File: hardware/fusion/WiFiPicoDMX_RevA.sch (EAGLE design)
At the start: 36 parts, among them J1 PANEL XLR-5: COM,-,+,SHELL, J2 PANEL DIN-5 MIDI IN, J3 FREE GPIO PADS, J4 ANALOG PADS, J5 RESERVED SIGNAL TEST PADS, J6 POWER/DMX TEST PADS, SW1 RESET (NO), U1 Raspberry Pi Pico 2 W, U2 ISOW1412DFMR, U3 6N138-500E

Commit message: Add validated hardware net lists
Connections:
- net 3V3_LOGIC renamed VCC_3V3_LOGIC
- net 5V_DMX_FUSED renamed VDD_5V_ISOW_FUSED
- net 5V_DMX_ISO renamed VCC_5V_DMX_ISO
- net 5V_DMX_ISO_RAW renamed VISO_5V_CONVERTER
- net 5V_VBUS_RAW renamed VBUS_5V_USB
- net DMX_LED_DRIVE renamed DMX_LED_ANODE
- net DMX_TRANSCEIVER_MINUS renamed DMX_TRX_MINUS
- net DMX_TRANSCEIVER_PLUS renamed DMX_TRX_PLUS
- net GND_DMX_ISO_RAW renamed GND_DMX_CONVERTER
- net GPIO0_FREE renamed GPIO0_EXP
- net GPIO10_FREE renamed GPIO10_EXP
- net GPIO11_FREE renamed GPIO11_EXP
- net GPIO12_FREE renamed GPIO12_EXP
- net GPIO13_FREE renamed GPIO13_EXP
- net GPIO14_FREE renamed GPIO14_EXP
- net GPIO15_FREE renamed GPIO15_EXP
- net GPIO16_FREE renamed GPIO16_EXP
- net GPIO17_FREE renamed GPIO17_EXP
- net GPIO18_FREE renamed GPIO18_EXP
- net GPIO19_FREE renamed GPIO19_EXP
- net GPIO1_FREE renamed GPIO1_EXP
- net GPIO20_FREE renamed GPIO20_EXP
- net GPIO21_FREE renamed GPIO21_EXP
- net GPIO22_FREE renamed GPIO22_EXP
- net GPIO8_FREE renamed GPIO8_EXP
- net GPIO9_FREE renamed GPIO9_EXP
- net ISOW_IN_NC renamed NC_U2_PIN14_IN
- net ISOW_OUT_NC renamed NC_U2_PIN7_OUT
- net MIDI_DIN_PIN1_NC renamed MIDI_DIN_PIN1_SPARE
- net MIDI_DIN_PIN3_NC renamed MIDI_DIN_PIN3_SPARE
- net MIDI_LED_ANODE renamed MIDI_OPTO_LED_ANODE
- net MIDI_LED_CATHODE renamed MIDI_OPTO_LED_CATHODE
- net PICO_3V3_EN renamed PICO_SMPS_EN
- net PICO_RUN renamed PICO_RUN_N
- net PWR_LED_DRIVE renamed PWR_LED_ANODE
- net U3_NC1 renamed NC_U3_PIN1
- net U3_NC4 renamed NC_U3_PIN4

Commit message: docs(hardware): select HCPL-0700 MIDI optocoupler
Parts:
- L1: value OPTIONAL CMC - DNP -> ACT45B-510-2P-TL003 - DNP
- SW1: value RESET (NO) -> PTS810SJM250SMTR LFS RESET (NO)
- U3: value 6N138-500E -> HCPL-0700-500E; device WiFiPicoDMX_RevA_embedded:6N138_500E -> WiFiPicoDMX_RevA_embedded:HCPL_0700_500E
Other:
- note added: "Default: FIT R10/R11 (0R), DNP L1. L1 option is TDK ACT45B-510-2P-TL003; fit it only after EMC/signal-integrity testing."
- note added: "HCPL-0700 output side uses 5V VCC with a 3.3V output pull-up. Verify timing/CTR on the assembled prototype."
- note removed: "6N138 output side uses 5V VCC with a 3.3V output pull-up. Verify timing/CTR on the assembled prototype."
- note removed: "FIT R10/R11 (0R) and DNP L1 until a common-mode choke is selected by EMC/signal-integrity testing."
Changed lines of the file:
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@@
         <part name="U1" library="WiFiPicoDMX_RevA_embedded" deviceset="PICO2W" device="" value="Raspberry Pi Pico 2 W"/>
         <part name="F1" library="WiFiPicoDMX_RevA_embedded" deviceset="PPTC1206" device="" value="1206L050YR 0.5A HOLD"/>
-        <part name="SW1" library="WiFiPicoDMX_RevA_embedded" deviceset="SWITCH_SMD" device="" value="RESET (NO)"/>
+        <part name="SW1" library="WiFiPicoDMX_RevA_embedded" deviceset="SWITCH_SMD" device="" value="PTS810SJM250SMTR LFS RESET (NO)"/>
         <part name="R8" library="WiFiPicoDMX_RevA_embedded" deviceset="RES0603" device="" value="1k"/>
         <part name="D3" library="WiFiPicoDMX_RevA_embedded" deviceset="LED0603" device="" value="PWR GREEN"/>
@@
         <part name="C5" library="WiFiPicoDMX_RevA_embedded" deviceset="CAP0805" device="" value="10u X7R VISOOUT"/>
         <part name="C6" library="WiFiPicoDMX_RevA_embedded" deviceset="CAP0402" device="" value="100n VISOIN"/>
-        <part name="L1" library="WiFiPicoDMX_RevA_embedded" deviceset="CMC_OPTION" device="" value="OPTIONAL CMC - DNP"/>
+        <part name="L1" library="WiFiPicoDMX_RevA_embedded" deviceset="CMC_OPTION" device="" value="ACT45B-510-2P-TL003 - DNP"/>
         <part name="R10" library="WiFiPicoDMX_RevA_embedded" deviceset="RES0603" device="" value="0R CMC BYPASS FIT"/>
         <part name="R11" library="WiFiPicoDMX_RevA_embedded" deviceset="RES0603" device="" value="0R CMC BYPASS FIT"/>
@@
         <part name="R5" library="WiFiPicoDMX_RevA_embedded" deviceset="RES0603" device="" value="220R"/>
         <part name="D2" library="WiFiPicoDMX_RevA_embedded" deviceset="DIODE_SOD323" device="" value="1N4148WS-E3-08"/>
-        <part name="U3" library="WiFiPicoDMX_RevA_embedded" deviceset="6N138_500E" device="" value="6N138-500E"/>
+        <part name="U3" library="WiFiPicoDMX_RevA_embedded" deviceset="HCPL_0700_500E" device="" value="HCPL-0700-500E"/>
         <part name="R6" library="WiFiPicoDMX_RevA_embedded" deviceset="RES0603" device="" value="4.7k OUTPUT PULLUP"/>
         <part name="R7" library="WiFiPicoDMX_RevA_embedded" deviceset="RES0603" device="" value="47k BASE SPEEDUP"/>
@@
                   <plain>
                     <text x="20.32" y="187.96" size="2.54" layer="91" ratio="15">WiFiPicoDMX Rev. A — Reinforced-isolated DMX/RDM output</text>
-                    <text x="20.32" y="20.32" size="1.778" layer="91" ratio="12">FIT R10/R11 (0R) and DNP L1 until a common-mode choke is selected by EMC/signal-integrity testing.</text>
+                    <text x="20.32" y="20.32" size="1.778" layer="91" ratio="12">Default: FIT R10/R11 (0R), DNP L1. L1 option is TDK ACT45B-510-2P-TL003; fit it only after EMC/signal-integrity testing.</text>
                     <text x="20.32" y="15.24" size="1.778" layer="91" ratio="12">No permanent 120R termination: terminate only at the far end of the DMX cable.</text>
                     <text x="20.32" y="10.16" size="1.778" layer="91" ratio="12">Keep GND_LOGIC and GND_DMX_ISO separate. Preserve TI isolation keep-outs and place bypass parts per TI layout.</text>
@@
                     <text x="20.32" y="187.96" size="2.54" layer="91" ratio="15">WiFiPicoDMX Rev. A — Isolated MIDI IN</text>
                     <text x="20.32" y="20.32" size="1.778" layer="91" ratio="12">J2 exposes all five panel DIN pins. Pins 1/3 are NC; pin 2 shield treatment remains configurable.</text>
-                    <text x="20.32" y="15.24" size="1.778" layer="91" ratio="12">6N138 output side uses 5V VCC with a 3.3V output pull-up. Verify timing/CTR on the assembled prototype.</text>
+                    <text x="20.32" y="15.24" size="1.778" layer="91" ratio="12">HCPL-0700 output side uses 5V VCC with a 3.3V output pull-up. Verify timing/CTR on the assembled prototype.</text>
                     <text x="20.32" y="10.16" size="1.778" layer="91" ratio="12">The DIN input current loop remains galvanically isolated from GND_LOGIC.</text>
                   </plain>

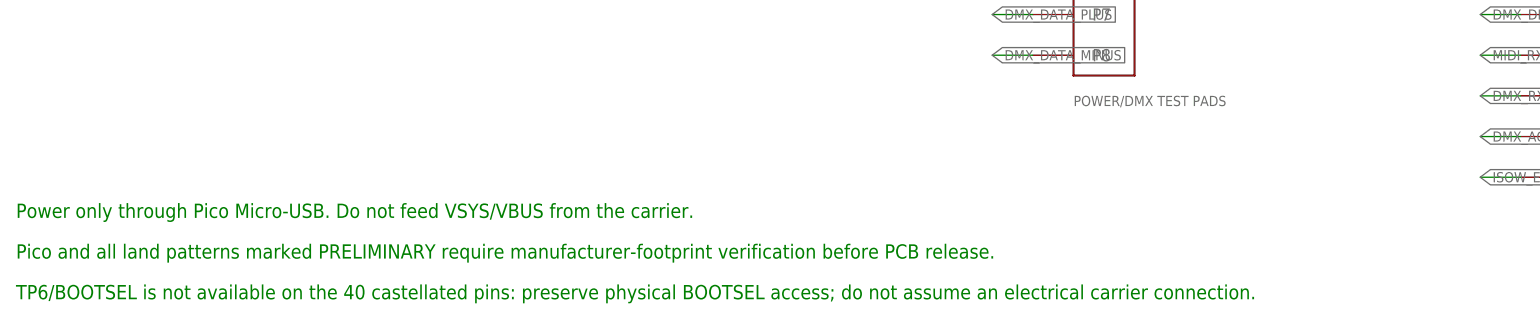
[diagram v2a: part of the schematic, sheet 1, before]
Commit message: feat(hardware): generate schematic from Fusion library
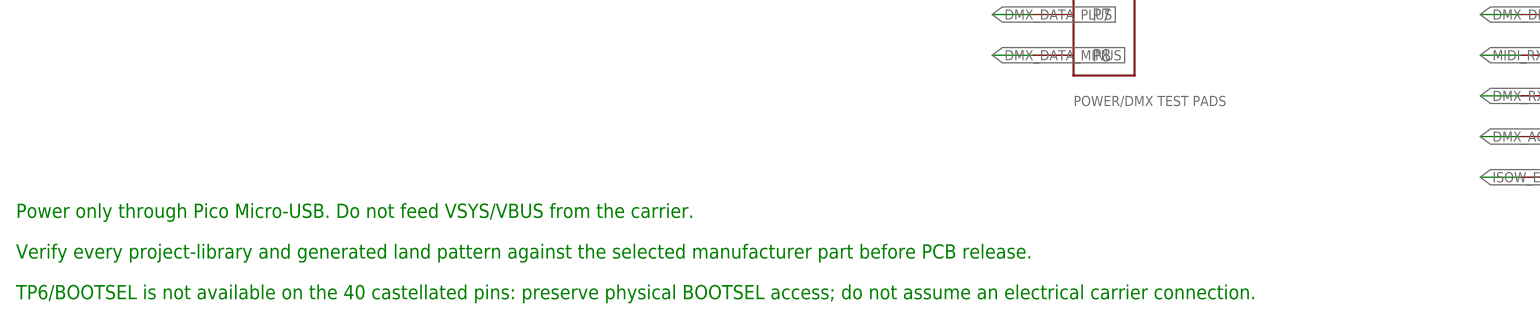
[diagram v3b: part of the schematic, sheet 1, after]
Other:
- note added: "Verify every project-library and generated land pattern against the selected manufacturer part before PCB release."
- note removed: "Pico and all land patterns marked PRELIMINARY require manufacturer-footprint verification before PCB release."
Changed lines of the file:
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@@
                     <text x="20.32" y="187.96" size="2.54" layer="91" ratio="15">WiFiPicoDMX Rev. A — Controller, power, controls and expansion</text>
                     <text x="20.32" y="15.24" size="1.778" layer="91" ratio="12">Power only through Pico Micro-USB. Do not feed VSYS/VBUS from the carrier.</text>
-                    <text x="20.32" y="10.16" size="1.778" layer="91" ratio="12">Pico and all land patterns marked PRELIMINARY require manufacturer-footprint verification before PCB release.</text>
+                    <text x="20.32" y="10.16" size="1.778" layer="91" ratio="12">Verify every project-library and generated land pattern against the selected manufacturer part before PCB release.</text>
                     <text x="20.32" y="5.08" size="1.778" layer="91" ratio="12">TP6/BOOTSEL is not available on the 40 castellated pins: preserve physical BOOTSEL access; do not assume an electrical carrier connection.</text>
                   </plain>

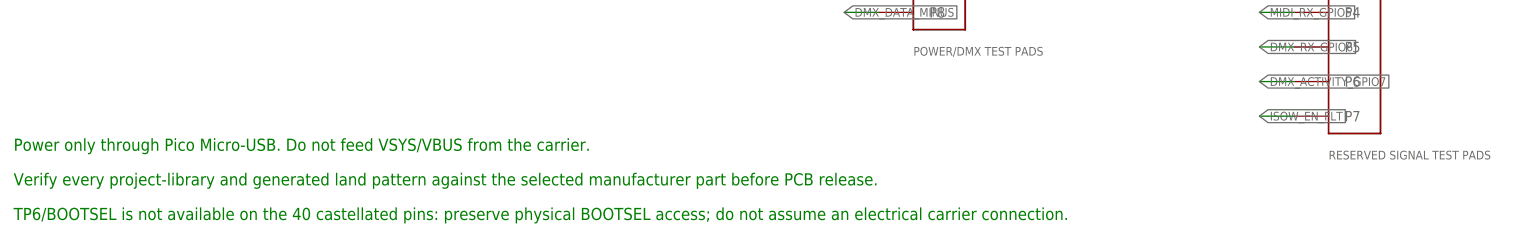
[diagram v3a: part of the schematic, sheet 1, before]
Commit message: fix(hardware): restore Fusion library models and Pico footprint
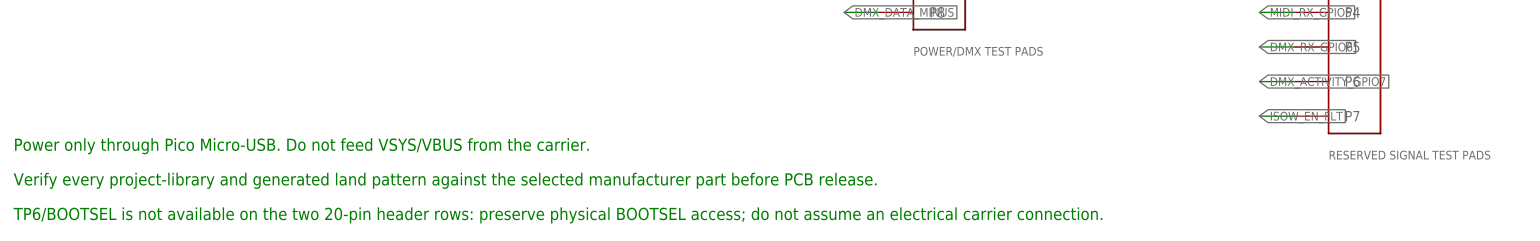
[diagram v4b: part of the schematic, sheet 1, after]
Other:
- note added: "TP6/BOOTSEL is not available on the two 20-pin header rows: preserve physical BOOTSEL access; do not assume an electrical carrier connection."
- note removed: "TP6/BOOTSEL is not available on the 40 castellated pins: preserve physical BOOTSEL access; do not assume an electrical carrier connection."
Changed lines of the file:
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@@
                     <text x="20.32" y="15.24" size="1.778" layer="91" ratio="12">Power only through Pico Micro-USB. Do not feed VSYS/VBUS from the carrier.</text>
                     <text x="20.32" y="10.16" size="1.778" layer="91" ratio="12">Verify every project-library and generated land pattern against the selected manufacturer part before PCB release.</text>
-                    <text x="20.32" y="5.08" size="1.778" layer="91" ratio="12">TP6/BOOTSEL is not available on the 40 castellated pins: preserve physical BOOTSEL access; do not assume an electrical carrier connection.</text>
+                    <text x="20.32" y="5.08" size="1.778" layer="91" ratio="12">TP6/BOOTSEL is not available on the two 20-pin header rows: preserve physical BOOTSEL access; do not assume an electrical carrier connection.</text>
                   </plain>
                   <instances>

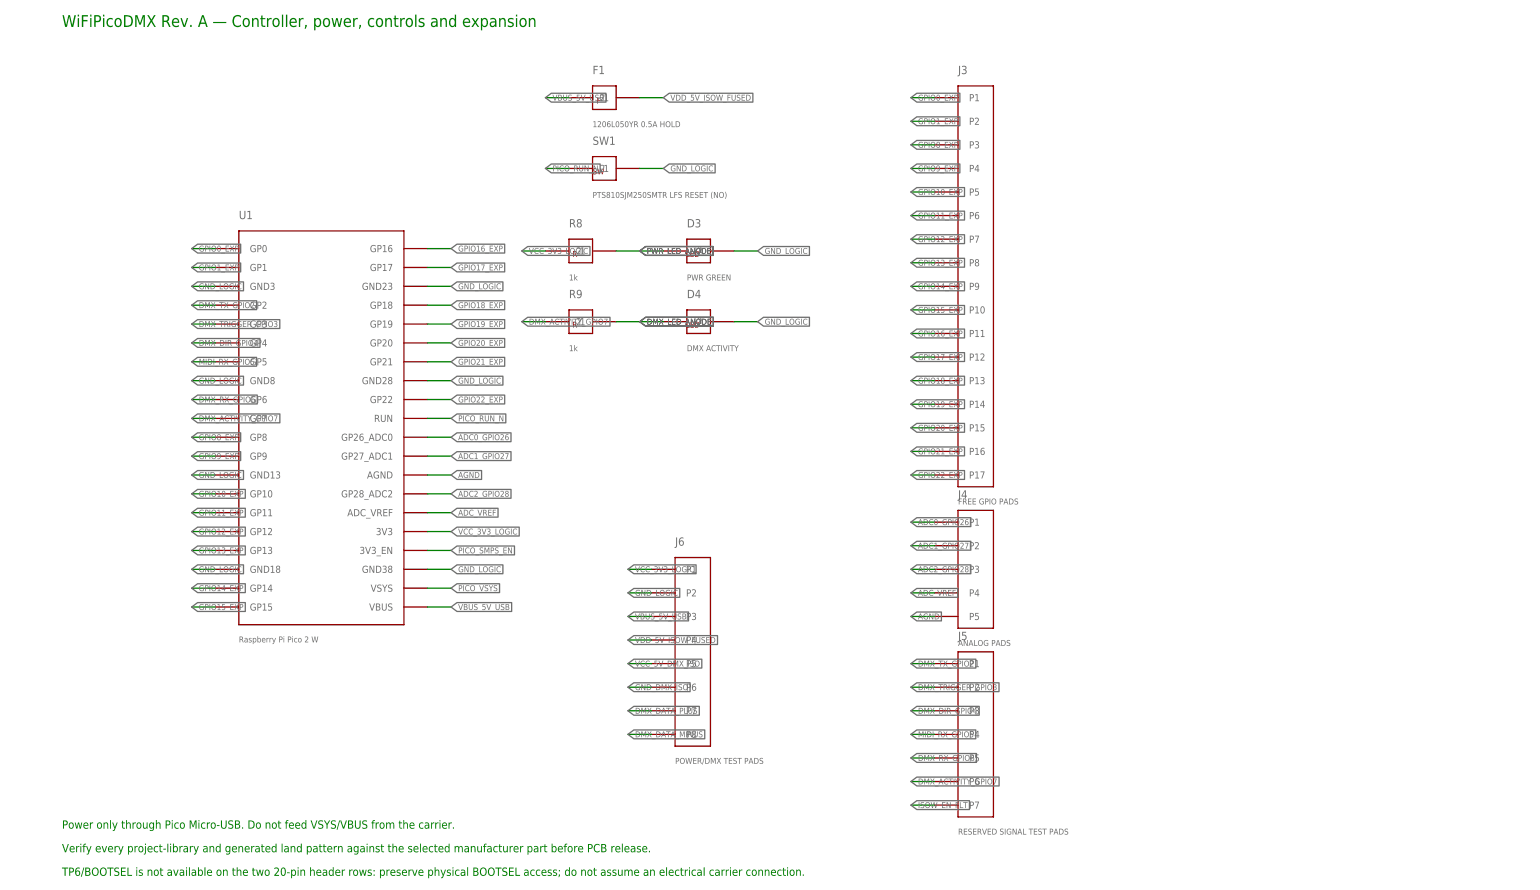
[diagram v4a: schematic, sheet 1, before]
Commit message: fix(hardware): improve generated Fusion schematic layout
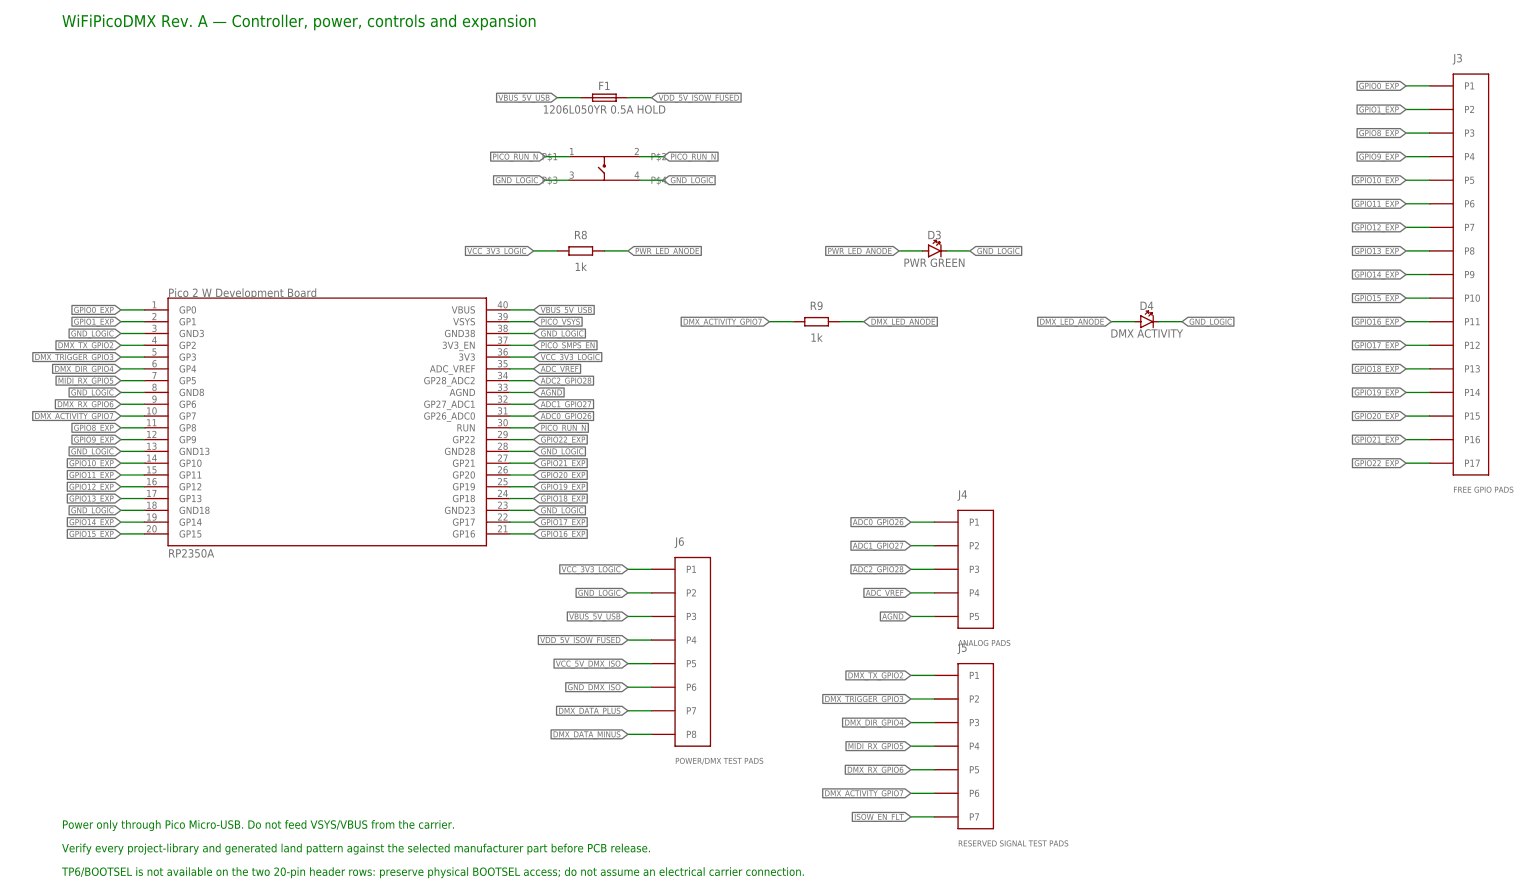
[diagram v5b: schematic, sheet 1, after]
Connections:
- net GND_LOGIC: now also SW1.P$3, SW1.P$4; no longer SW1.2
- net PICO_RUN_N: now also SW1.P$1, SW1.P$2; no longer SW1.1
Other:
- moved on the sheet: D1, J1, J3, J5, L1

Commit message: hardware: freeze Rev A passive BOM
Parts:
- added C8: 1uF 50V 10% X5R 0603 CL10A105KB8NNNC VDD 2-4mm, WiFiPicoDMX_RevA_embedded:CAP0603
- added C9: 1uF 50V 10% X5R 0603 CL10A105KB8NNNC VISOOUT 2-4mm, WiFiPicoDMX_RevA_embedded:CAP0603
- C1: value 100n VIO -> 100nF 16V 10% X7R 0402 CL05B104KO5NNNC VIO
- C2: value 10n VDD <=1mm -> 10nF 50V 10% X7R 0402 0402B103K500CT VDD <1mm
- C3: value 10u X7R VDD -> 10uF 35V 10% X5R 0805 GRM21BR6YA106KE43L VDD
- C4: value 10n VISOOUT <=1mm -> 10nF 50V 10% X7R 0402 0402B103K500CT VISOOUT <1mm
- C5: value 10u X7R VISOOUT -> 10uF 35V 10% X5R 0805 GRM21BR6YA106KE43L VISOOUT
- C6: value 100n VISOIN -> 100nF 16V 10% X7R 0402 CL05B104KO5NNNC VISOIN
- C7: value 100n VCC -> 100nF 16V 10% X7R 0402 CL05B104KO5NNNC MIDI VCC
- D3: value PWR GREEN -> PWR GREEN Lite-On LTST-C190KGKT
- D4: value DMX ACTIVITY -> DMX YELLOW Lite-On LTST-C190KSKT
- R1: value 100k D PULLUP -> 100k 1% 0.063W 0402 Yageo RC0402FR-07100KL
- R10, R11: value 0R CMC BYPASS FIT -> 0R 5% 0.1W 0603 Yageo RC0603JR-070RL CMC BYPASS FIT
- R2: value 10k DIR PULLDOWN -> 10k 1% 0.063W 0402 Yageo RC0402FR-0710KL
- R3: value 10k EN/FLT PULLUP -> 10k 1% 0.063W 0402 Yageo RC0402FR-0710KL
- R4, R5: value 220R -> 220R 1% 0.1W 0603 Yageo RC0603FR-07220RL
- R6: value 4.7k OUTPUT PULLUP -> 4.7k 1% 0.1W 0603 Yageo RC0603FR-074K7L
- R7: value 47k BASE SPEEDUP -> 47k 1% 0.1W 0603 Yageo RC0603FR-0747KL
- R8, R9: value 1k -> 1k 1% 0.1W 0603 Yageo RC0603FR-071KL
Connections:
- net GND_DMX_CONVERTER: now also C9.2
- net GND_LOGIC: now also C8.2
- net VDD_5V_ISOW_FUSED: now also C8.1
- net VISO_5V_CONVERTER: now also C9.1
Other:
- note added: "Use the Pico 2 W development board's onboard BOOTSEL button below the USB connector; preserve finger/tool access in the PCB and enclosure."
- note removed: "TP6/BOOTSEL is not available on the two 20-pin header rows: preserve physical BOOTSEL access; do not assume an electrical carrier connection."
